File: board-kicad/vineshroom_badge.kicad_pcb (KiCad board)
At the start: 2 copper layers, 95 x 95.7 mm, 78 parts, among them IC1 ATTINY20-X, J1 CONN-TAGCONNECT-TC2050, Q1 Q_NMOS_DGS, SW1 SW_SPST

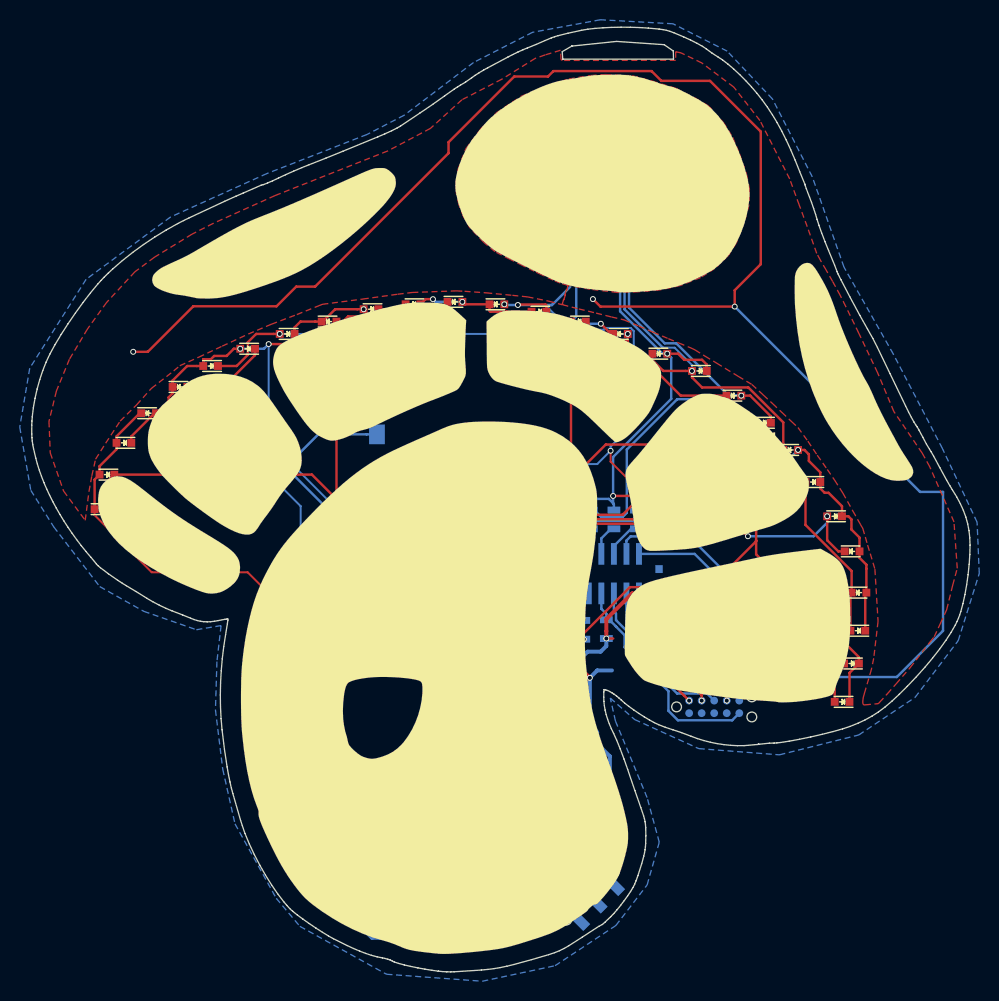
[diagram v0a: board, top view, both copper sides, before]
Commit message: fixed pinout on programming header, some other shit too whatever lets get this done
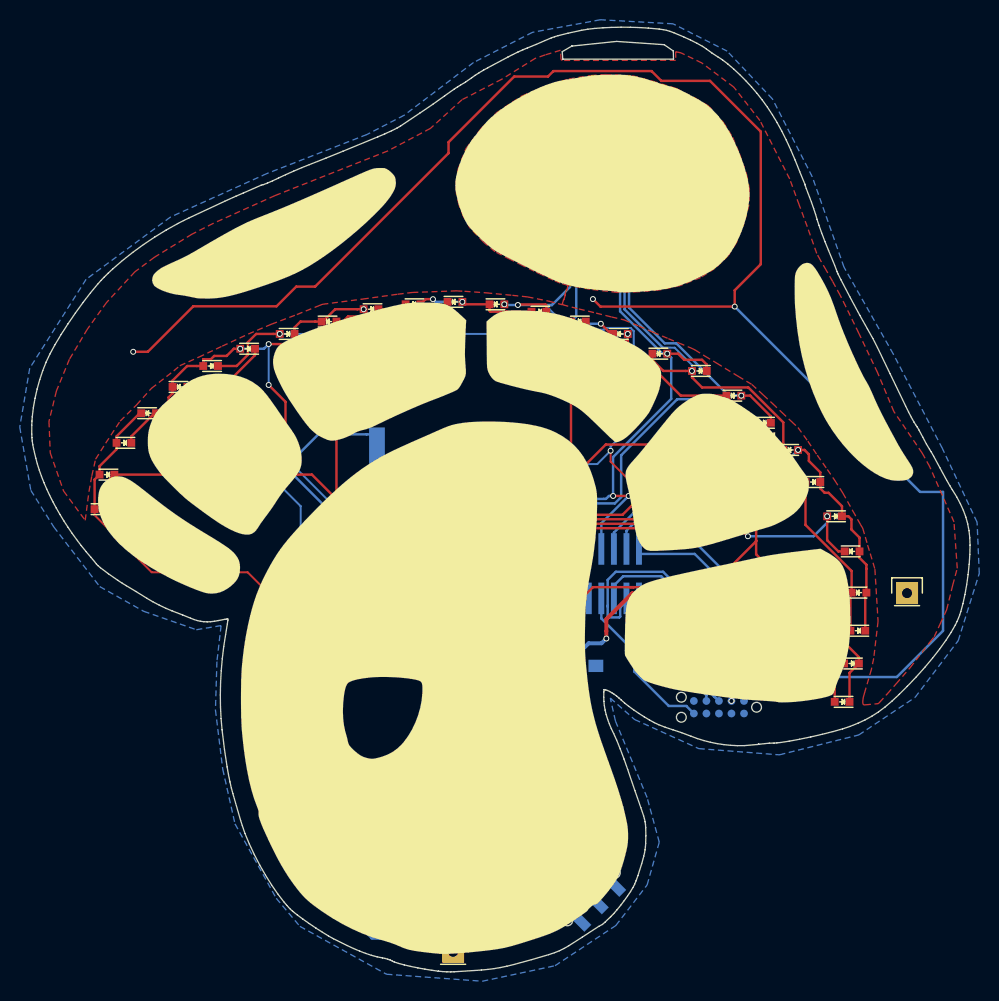
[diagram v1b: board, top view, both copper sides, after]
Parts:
- removed ON/OFF: SW_DPDT_x2, vine_badge:JS202011JAQN
- removed Q1: Q_NMOS_DGS, TO_SOT_Packages_SMD:SOT-23
- removed R1, R2, R3, R4, R5, R6, R7, R8: R, Resistors_SMD:R_0805
- added D53: D_Schottky, Diodes_SMD:SOD-323_HandSoldering, B.Cu at (152.7, 122.2)
- added ON/OFF1: SW_DPDT_x2, vine_badge:JS202011JAQN, B.Cu at (151.1, 134.4)
- added TP_BATT1: TEST, Pin_Headers:Pin_Header_Straight_1x01, F.Cu at (137.2, 140.0)
- added TP_GND1: TEST, Pin_Headers:Pin_Header_Straight_1x01, F.Cu at (183.1, 103.6)
- C1, C2: footprint Capacitors_SMD:C_0603 -> Capacitors_SMD:C_0805_HandSoldering
- IC1: footprint spang_badge:ATTINY20_SOIC-14 -> vine_badge:ATTINY20_SOIC-14-HANDSOLDER
- R10, R9: footprint Resistors_SMD:R_0805 -> Resistors_SMD:R_0805_HandSoldering
- SW1: footprint Buttons_Switches_SMD:SW_SPST_EVQPE1 -> vine_badge:SW_SPST_EVQPE1
- moved F1 13.8 mm to (153.4, 127.0), turned to 270 degrees
- moved C1 6.30 mm to (150.4, 111.0), turned to 0 degrees
- moved R9 4.96 mm to (156.5, 110.5), turned to 315 degrees
- moved C2 2.72 mm to (157.7, 104.6)
- moved R10 0.50 mm to (144.8, 103.7)
- moved J1 0.48 mm to (164.1, 115.2), turned to 180 degrees
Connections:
- BT1 pad 2: Net-(BT1-Pad2) -> GND
- F1 pad 1: +BATT -> Net-(D53-Pad2)
- IC1 pad 10: Net-(IC1-Pad10) -> Net-(D10-Pad2)
- IC1 pad 11: Net-(IC1-Pad11) -> Net-(D10-Pad1)
- IC1 pad 12: Net-(IC1-Pad12) -> Net-(D1-Pad1)
- IC1 pad 13: Net-(IC1-Pad13) -> Net-(D1-Pad2)
- IC1 pad 6: Net-(IC1-Pad6) -> Net-(D14-Pad2)
- IC1 pad 7: Net-(IC1-Pad7) -> Net-(D13-Pad2)
- IC1 pad 8: Net-(IC1-Pad8) -> Net-(D12-Pad2)
- IC1 pad 9: Net-(IC1-Pad9) -> Net-(D11-Pad2)
- J1 pad 1: /TCK -> Net-(J1-Pad1)
- J1 pad 10: Net-(J1-Pad10) -> /TCK
- J1 pad 2: GND -> Net-(J1-Pad2)
- J1 pad 3: /TDI -> Net-(J1-Pad3)
- J1 pad 4: +BATT -> Net-(J1-Pad4)
- J1 pad 5: Net-(J1-Pad5) -> /RST
- J1 pad 6: /RST -> Net-(J1-Pad6)
- J1 pad 7: Net-(J1-Pad7) -> +BATT
- J1 pad 8: Net-(J1-Pad8) -> /TDI
- J1 pad 9: Net-(J1-Pad9) -> GND
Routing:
- net GND: track 234.2 -> 192.9 mm, vias 7 -> 4
- net Net-(BT1-Pad2): track 32.3 -> 0.00 mm
- net /TCK: track 14.5 -> 31.4 mm, vias 2 -> 0
- net Net-(F1-Pad2): track 20.7 -> 4.09 mm
- net +BATT: track 55.0 -> 39.4 mm, vias 3 -> 2
- net Net-(D1-Pad2): track 143.9 -> 151.3 mm
- net Net-(D10-Pad1): track 189.0 -> 195.6 mm, vias 8 -> 9
- net Net-(D1-Pad1): track 105.0 -> 110.7 mm
- net Net-(IC1-Pad13): track 5.14 -> 0.00 mm
- net Net-(D11-Pad2): track 103.8 -> 108.8 mm
- net Net-(D12-Pad2): track 137.2 -> 141.9 mm
- net Net-(D10-Pad2): track 150.4 -> 154.6 mm
- net Net-(IC1-Pad12): track 3.81 -> 0.00 mm
- net Net-(IC1-Pad8): track 3.60 -> 0.00 mm
- net /TDI: track 17.6 -> 21.1 mm
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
